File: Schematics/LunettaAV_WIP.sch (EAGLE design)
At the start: 64 parts, among them IC1 TLC339P, IC2 7805, IC3 4046N, IC4 4040N, IC5 4017N, IC6 4051N, IC7 4094N, IC8 4046N, IC9 40106N, J1 POWER_JACKPOWER_JACK_SLOT, U1 LM358, U2 LM358

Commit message: PT Delay and other fixes
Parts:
- removed JP7: (no value), pinhead:PINHD-1X3
- added C14: .1uF, capacitor-wima:C2.5/2
- added C15, C16, C17, C19, C20, C21, C22: 0.1uF, SparkFun-Capacitors:0.1UF-KIT-EZ-50V-20%
- added C18: 47uF, SparkFun-Capacitors:10UF-POLAR-RADIAL-2.5MM-25V-20%
- added C23: 100uF, SparkFun-Capacitors:100UF-POLAR-RADIAL-2.5MM-25V-20%
- added CLOCK-OUT, J3: WQP-PJ301M-12_JACK, MusicThingModular:WQP-PJ301M-12_JACK
- added D1: BAT42, diode:BAT42
- added J2: (no value), SparkFun-Connectors:CONN_04LONGPADS
- added R20: 10K, MusicThingModular:RESISTOR7MM
- added R21: (no value), MusicThingModular:RESISTOR7MM
- added VR5: (no value), MusicThingModular:9MM_SNAP-IN_POT_
- C1: value 10nF -> 0.1uF; device SparkFun-Capacitors:10NF-PTH-10MM-10000V-1-% -> SparkFun-Capacitors:0.1UF-KIT-EZ-50V-20%
- C10: value 10uF -> 10nF; device SparkFun-Capacitors:10UF-POLAR-RADIAL-2.5MM-25V-20% -> SparkFun-Capacitors:10NF-PTH-10MM-10000V-1-%
- C11: value 47uF -> 0.1uF; device SparkFun-Capacitors:10UF-POLAR-RADIAL-2.5MM-25V-20% -> SparkFun-Capacitors:0.1UF-KIT-EZ-50V-20%
- C2: value .1uF -> 10uF; device capacitor-wima:C2.5/2 -> SparkFun-Capacitors:10UF-POLAR-RADIAL-2.5MM-25V-20%
- C3: value 100uF -> 10uF; device SparkFun-Capacitors:100UF-POLAR-RADIAL-2.5MM-25V-20% -> SparkFun-Capacitors:10UF-POLAR-RADIAL-2.5MM-25V-20%
- C5: value 0.1uF -> 10uF; device SparkFun-Capacitors:0.1UF-KIT-EZ-50V-20% -> SparkFun-Capacitors:10UF-POLAR-RADIAL-2.5MM-25V-20%
- C8, C9: value 10uF -> 0.1uF; device SparkFun-Capacitors:10UF-POLAR-RADIAL-2.5MM-25V-20% -> SparkFun-Capacitors:0.1UF-KIT-EZ-50V-20%
- IC1: value TLC339P -> 7809\; device linear:TLC339P -> v-reg:78XXS
- IC10: value (none) -> 4051N; device v-reg:78XXS -> 40xx:4051N
- IC3: value 4046N -> 4040N; device 40xx:4046N -> 40xx:4040N
- IC4: value 4040N -> TLC339P; device 40xx:4040N -> linear:TLC339P
- IC5: value 4017N -> 4046N; device 40xx:4017N -> 40xx:4046N
- IC6: value 4051N -> 4094N; device 40xx:4051N -> 40xx:4094N
- IC7: value 4094N -> 40106N; device 40xx:4094N -> 40xx:40106N
- IC9: value 40106N -> 4017N; device 40xx:40106N -> 40xx:4017N
- JP1: device adafruit:PINHD-2X4 -> pinhead:PINHD-1X2
- JP2: device pinhead:PINHD-1X2 -> adafruit:PINHD-2X4
- JP4: device adafruit:PINHD-2X4 -> pinhead:PINHD-2X8
- JP5: device pinhead:PINHD-2X8 -> pinhead:PINHD-1X3
- R1, R2: value 10K -> 4.7K; device MusicThingModular:RESISTOR7MM -> MusicThingModular:RESISTOR10MM_RESISTOR
- R13: value (none) -> 1K
- R14: value 10K -> 1K
- R15: value 10K -> LDR; device MusicThingModular:RESISTOR7MM -> rcl:R-EU_0204/2V
- R16: value 10K -> 100k
- R17: value 1K -> 10k
- R18: value 10k -> 10K
- R19: value 100k -> 10K
- R22: value 1K -> (none)
- R23: value LDR -> (none); device rcl:R-EU_0204/2V -> MusicThingModular:RESISTOR7MM
- R3: value 10K -> 1K; device MusicThingModular:RESISTOR7MM -> MusicThingModular:RESISTOR10MM_RESISTOR
- R5: value 1K -> 10K; device MusicThingModular:RESISTOR10MM_RESISTOR -> MusicThingModular:RESISTOR7MM
- R6, R9: value 4.7K -> 10K; device MusicThingModular:RESISTOR10MM_RESISTOR -> MusicThingModular:RESISTOR7MM
- VR3: value (none) -> 100K
- VR4: value 100K -> (none)
- renumbered U$1 to OL96$1, U$2 to OL96$2
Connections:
- new net N$31: C19.2, DD1.11
- new net N$32: CLOCK-OUT.2, D1.C
- new net OUT: VR5.S
- net 3V3: now also C1.1, C4.1, R1.2, R2.2, R5.2; no longer C12.1, C13.1, R10.2, R11.2, R9.2
- net 5V: now also C23.+, C5.+, IC4A.-IN, IC4B.-IN, IC4C.-IN, IC4D.-IN, JP1.1; no longer C3.+, C9.+, IC1A.-IN, IC1B.-IN, IC1C.-IN, IC1D.-IN, JP2.1
- net 9V: now also C11.1, C12.1, C13.1, C15.1, C16.1, C17.1, C3.+, C6.1, C7.1, C8.1, C9.1, IC1.OUT, IC10P.VCC, IC4P.V+, IC6A.OE, IC6A.STR, IC6P.VDD, IC9P.VDD, R13.1; no longer C8.+, IC10.OUT, IC1P.V+, IC4P.VDD, IC6P.VCC, IC7A.OE, IC7A.STR, R22.1
- net ANALOGIN1: no longer U1G1.+IN
- net ANALOGIN2: now also U1G1.+IN
- net AUDIORATE: now also IC7C.O, IC9A.CLK; no longer IC5A.CLK, IC9C.O
- net BUFFCLOCK: now also IC6A.CLK, R22.1; no longer IC7A.CLK
- net BUFFMEL: now also R16.1, VR5.E; no longer R19.1
- net CLOCKSELECT: now also JP2.2, JP2.4, JP2.6, JP2.8; no longer JP4.2, JP4.4, JP4.6, JP4.8
- net DCIN: now also C2.+, IC1.IN; no longer C10.+, IC10.IN
- net DIN1: now also R3.2; no longer R5.2
- net GND: now also C1.2, C11.2, C14.2, C15.2, C16.2, C17.2, C18.-, C19.1, C2.-, C20.1, C22.2, C23.-, C5.-, C6.2, C7.2, C8.2, C9.2, CLOCK-OUT.1, DD1.12, IC1.GND, IC10A.INH, IC10P.GND, IC10P.VEE, IC4P.V-, IC5A.INH, IC6P.VSS, IC7D.I, IC7E.I, IC7F.I, IC9A.ENA, IC9P.VSS, R10.1, R11.1, R18.1, R19.1, R20.1, R23.2, R9.1, VR4.A, VR5.A; no longer C10.-, C11.-, C2.2, C5.1, C8.-, C9.-, IC10.GND, IC1P.V-, IC3A.INH, IC4P.VSS, IC5A.ENA, IC6A.INH, IC6P.GND, IC6P.VEE, IC9D.I, IC9E.I, IC9F.I, R1.1, R14.1, R15.1, R16.1, R2.1, R5.1
- net MELODYOUT: now also IC9A.Q0; no longer IC5A.Q0
- net MOOX: now also IC10A.C, JP5.3, R20.2; no longer IC6A.C, JP7.3, R16.2
- net MOXO: now also IC10A.B, JP5.2, R19.2; no longer IC6A.B, JP7.2, R15.2
- net MXOO: now also IC10A.A, JP5.1, R18.2; no longer IC6A.A, JP7.1, R14.2
- net N$1: now also JP1.2; no longer JP2.2
- net N$10: now also IC7B.O, IC7C.I; no longer IC9B.O, IC9C.I
- net N$11: now also C14.1, IC7A.I, R15.2, VR3.S; no longer C2.1, IC9A.I, R23.2, VR4.S
- net N$12: now also C21.1; no longer C6.1
- net N$13: now also R22.2, R23.1, U2G1.+IN; no longer C7.2, DD1.11
- net N$14: now also D1.A, U2G1.-IN, U2G1.OUT; no longer C7.1, DD1.12
- net N$15: now also R21.2; no longer R13.2
- net N$16: now also C18.+; no longer C11.+
- net N$17: now also C20.2; no longer C5.2
- net N$18: now also C22.1; no longer C4.1
- net N$19: now also IC10A.X, IC9A.RES; no longer IC5A.RES, IC6A.X
- net N$2: now also C10.2, IC5A.CX@2; no longer C1.2, IC3A.CX@2
- net N$20: now also IC10A.X0, IC9A.Q2; no longer IC5A.Q2, IC6A.X0
- net N$21: now also IC10A.X1, IC9A.Q3; no longer IC5A.Q3, IC6A.X1
- net N$22: now also IC10A.X2, IC9A.Q4; no longer IC5A.Q4, IC6A.X2
- net N$23: now also IC10A.X3, IC9A.Q5; no longer IC5A.Q5, IC6A.X3
- net N$24: now also IC10A.X4, IC9A.Q6; no longer IC5A.Q6, IC6A.X4
- net N$25: now also IC10A.X5, IC9A.Q7; no longer IC5A.Q7, IC6A.X5
- net N$26: now also IC10A.X6, IC9A.Q8; no longer IC5A.Q8, IC6A.X6
- net N$27: now also IC10A.X7, IC9A.Q9; no longer IC5A.Q9, IC6A.X7
- net N$28: now also IC6A.D, R14.1; no longer IC7A.D, R17.1
- net N$29: now also R16.2, R17.1; no longer R18.1, R19.2
- net N$3: now also R1.1; no longer R6.1
- net N$30: now also R17.2, VR4.S; no longer R18.2
- net N$4: now also R2.1; no longer R9.1
- net N$5: now also C10.1, IC5A.CX@1; no longer C1.1, IC3A.CX@1
- net N$6: now also IC5A.R1; no longer IC3A.R1
- net N$7: now also C21.2; no longer C6.2
- net N$8: now also R13.2; no longer R22.2
- net N$9: now also IC7A.O, IC7B.I, R15.1, VR3.E; no longer IC9A.O, IC9B.I, R23.1, VR4.E
- net OOX: now also IC4D.+IN, J2.4, R11.2; no longer IC1D.+IN, JP1.1, JP1.2, R8.2
- net OXO: now also IC4C.+IN, J2.3, R10.2; no longer IC1C.+IN, JP1.3, JP1.4, R3.2
- net PLL/16: now also IC3A.Q4; no longer IC4A.Q4
- net PLL/2: now also IC3A.Q1, JP2.3; no longer IC4A.Q1, JP4.3
- net PLL/32: now also IC3A.Q5; no longer IC4A.Q5
- net PLL/4: now also IC3A.Q2, JP2.5; no longer IC4A.Q2, JP4.5
- net PLL/8: now also IC3A.Q3, JP2.7; no longer IC4A.Q3, JP4.7
- net PLLCLOCKOUT: now also IC3A.P1, IC5A.VCOOUT, JP2.1; no longer IC3A.VCOOUT, IC4A.P1, JP4.1
- net RESET: now also IC4A.+IN, J2.1, R8.2; no longer IC1A.+IN, JP1.7, JP1.8, R1.2
- net SPEEDYBUFF: now also IC5A.VCOIN; no longer IC3A.VCOIN
- net SR1: now also IC6A.Q1, JP4.1, JP4.2; no longer IC7A.Q1, JP5.1, JP5.2
- net SR2: now also IC6A.Q2, JP4.3, JP4.4; no longer IC7A.Q2, JP5.3, JP5.4
- net SR3: now also IC6A.Q3, JP4.5, JP4.6; no longer IC7A.Q3, JP5.5, JP5.6
- net SR4: now also IC6A.Q4, JP4.7, JP4.8; no longer IC7A.Q4, JP5.7, JP5.8
- net SR5: now also IC6A.Q5, JP4.10, JP4.9; no longer IC7A.Q5, JP5.10, JP5.9
- net SR6: now also IC6A.Q6, JP4.11, JP4.12; no longer IC7A.Q6, JP5.11, JP5.12
- net SR7: now also IC6A.Q7, JP4.13, JP4.14; no longer IC7A.Q7, JP5.13, JP5.14
- net SR8: now also IC6A.Q8, JP4.15, JP4.16, R14.2; no longer IC7A.Q8, JP5.15, JP5.16, R17.2
- net TNSYOOX: now also IC4D.OUT, R7.1; no longer IC1D.OUT, R11.1
- net TNSYOXO: now also IC4C.OUT, R6.1; no longer IC1C.OUT, R10.1
- net TNSYRES: now also IC4A.OUT; no longer IC1A.OUT
- net TNSYXOO: now also IC4B.OUT, R5.1; no longer IC1B.OUT, R7.1
- net XOO: now also IC4B.+IN, J2.2, R9.2; no longer IC1B.+IN, JP1.5, JP1.6, R2.2
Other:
- note removed: "Buffer the Mix (LM358)"
- note removed: "Final Mix"
- note removed: "Send to PT2399"
- moved on the sheet: C1, IC3P, IC7P, IC8P, IC9P, R1, R10, R11, R13, R14, R15, R16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

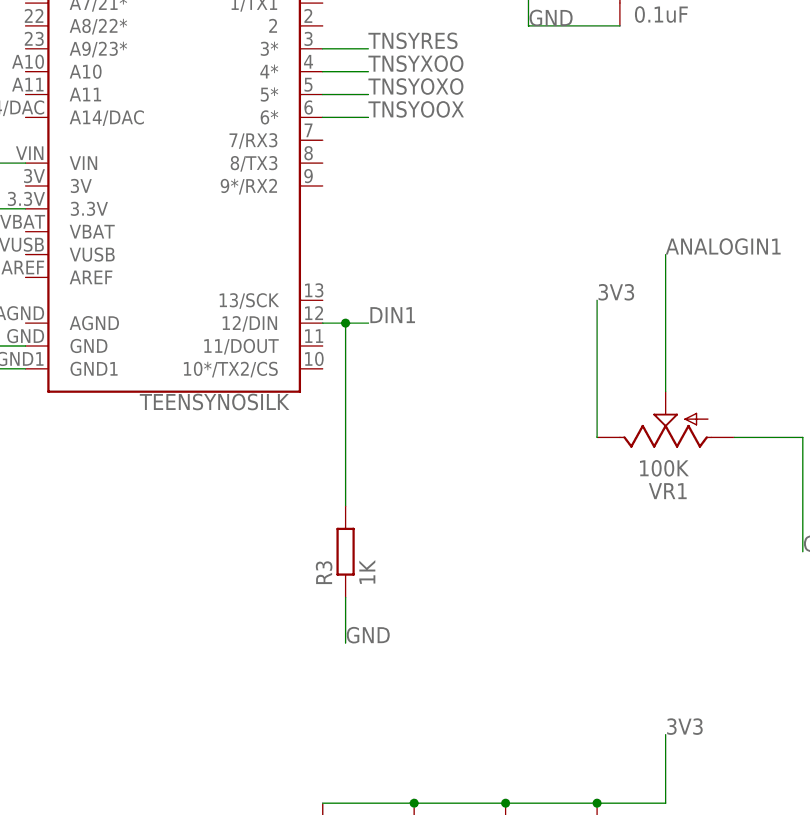
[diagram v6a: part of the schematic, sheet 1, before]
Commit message: update schematics to match new code
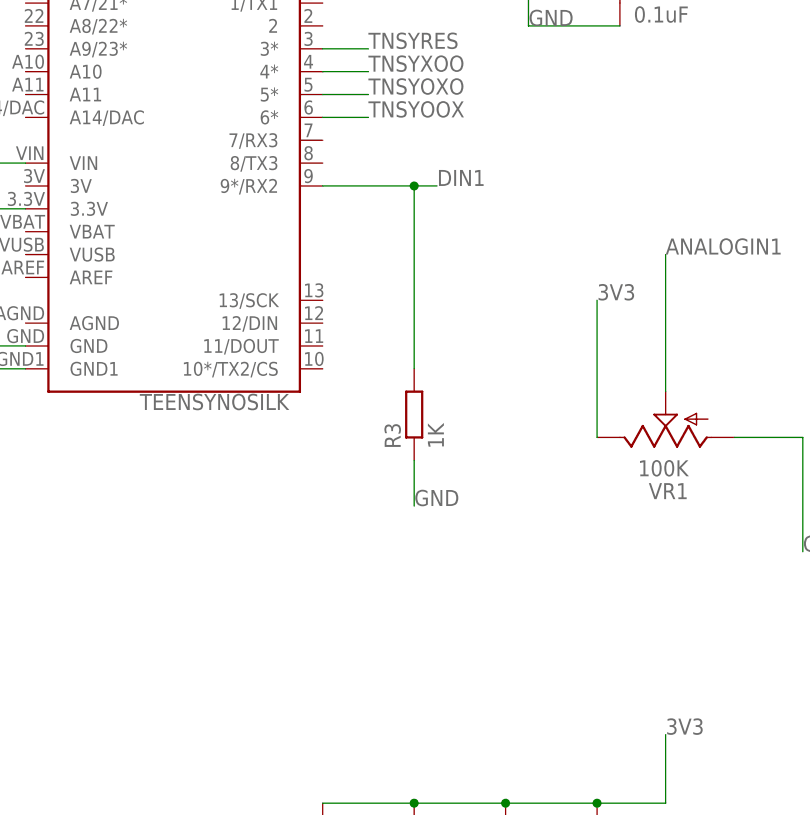
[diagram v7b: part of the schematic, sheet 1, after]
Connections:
- net DIN1: now also B1.9*/RX2; no longer B1.12/DIN
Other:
- moved on the sheet: R3
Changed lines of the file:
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@@
 <attribute name="VALUE" x="35.56" y="60.96" size="1.778" layer="96" rot="R180"/>
 </instance>
-<instance part="R3" gate="G$1" x="-35.56" y="50.8" smashed="yes" rot="R90">
-<attribute name="NAME" x="-37.0586" y="46.99" size="1.778" layer="95" rot="R90"/>
-<attribute name="VALUE" x="-32.258" y="46.99" size="1.778" layer="96" rot="R90"/>
+<instance part="R3" gate="G$1" x="-27.94" y="66.04" smashed="yes" rot="R90">
+<attribute name="NAME" x="-29.4386" y="62.23" size="1.778" layer="95" rot="R90"/>
+<attribute name="VALUE" x="-24.638" y="62.23" size="1.778" layer="96" rot="R90"/>
 </instance>
 <instance part="FRAME1" gate="G$1" x="-142.24" y="-76.2" smashed="yes">
@@
 <segment>
 <pinref part="R3" gate="G$1" pin="1"/>
-<wire x1="-35.56" y1="45.72" x2="-35.56" y2="40.64" width="0.1524" layer="91"/>
-<label x="-35.56" y="40.64" size="1.778" layer="95"/>
+<wire x1="-27.94" y1="60.96" x2="-27.94" y2="55.88" width="0.1524" layer="91"/>
+<label x="-27.94" y="55.88" size="1.778" layer="95"/>
 </segment>
 <segment>
@@
 <net name="DIN1" class="0">
 <segment>
-<pinref part="B1" gate="G$1" pin="12/DIN"/>
-<wire x1="-38.1" y1="76.2" x2="-35.56" y2="76.2" width="0.1524" layer="91"/>
-<label x="-33.02" y="76.2" size="1.778" layer="95"/>
+<label x="-25.4" y="91.44" size="1.778" layer="95"/>
 <pinref part="R3" gate="G$1" pin="2"/>
-<wire x1="-35.56" y1="76.2" x2="-33.02" y2="76.2" width="0.1524" layer="91"/>
-<wire x1="-35.56" y1="55.88" x2="-35.56" y2="76.2" width="0.1524" layer="91"/>
-<junction x="-35.56" y="76.2"/>
-</segment>
-<segment>
+<wire x1="-27.94" y1="91.44" x2="-25.4" y2="91.44" width="0.1524" layer="91"/>
+<wire x1="-27.94" y1="71.12" x2="-27.94" y2="91.44" width="0.1524" layer="91"/>
+<pinref part="B1" gate="G$1" pin="9*/RX2"/>
+<wire x1="-27.94" y1="91.44" x2="-38.1" y2="91.44" width="0.1524" layer="91"/>
+<junction x="-27.94" y="91.44"/>
+</segment>
+<segment>

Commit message: finish schematics?
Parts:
- removed VR2, VR3: 100K, MusicThingModular:9MM_SNAP-IN_POT_
- added C24: 10uF, SparkFun-Capacitors:10UF-POLAR-RADIAL-2.5MM-25V-20%
- added D2: BAT42, diode:BAT42
- added DENSITY, PITCH, SPEED: 100K, MusicThingModular:9MM_SNAP-IN_POT_
- added LED1, LED2: (no value), led:LED3MM
- added R24, R25, R26: 4.7k, MusicThingModular:RESISTOR7MM
- added R27, R28, R30, R31: 100k, MusicThingModular:RESISTOR7MM
- added R29, R32: 10k, MusicThingModular:RESISTOR7MM
- added T1, T2: (no value), transistor-neu-to92:2N4401-NPN-TO92-EBC
- added U3: MICROCHIP_MCP41050-I-PMICROCHIP_MCP41050-I-P_0_0, MCP41050:MICROCHIP_MCP41050-I-PMICROCHIP_MCP41050-I-P_0_0
- C10: value 10nF -> 0.1uF; device SparkFun-Capacitors:10NF-PTH-10MM-10000V-1-% -> SparkFun-Capacitors:0.1UF-KIT-EZ-50V-20%
- JP5: device pinhead:PINHD-1X3 -> jumper:JP4E
- R1, R2, R3: device MusicThingModular:RESISTOR10MM_RESISTOR -> MusicThingModular:RESISTOR7MM
- R21: value (none) -> 2.2k
- R22, R23: value (none) -> 100k
- VR1: value 100K -> (none); device MusicThingModular:9MM_SNAP-IN_POT_ -> MusicThingModular:BOURNS_3362P_TRIMMERP
- renumbered VR4 to FDBCK, VR5 to MIX
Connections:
- new net DPOTDATA: B1.11/DOUT, R25.1, U3.SI
- new net DPOTSCK: B1.13/SCK, R26.1, U3.SCK
- new net DPOTSEL: B1.10*/TX2/CS, R24.1, U3.!CS!
- new net LDRIVER: JP5.4, R30.1
- new net N$33: R21.1, U3.PA0
- new net N$34: R27.2, R28.2, T1.B
- new net N$35: R29.1, T1.C
- new net N$36: LED1.C, R29.2
- new net N$37: R30.2, R31.2, T2.B
- new net N$38: R32.1, T2.C
- new net N$39: LED2.C, R32.2
- new net N$40: J3.2, VR1.2
- new net N$41: C24.-, VR1.1
- net 3V3: now also DENSITY.E, SPEED.E; no longer VR1.E, VR2.E
- net 5V: now also R24.2, R25.2, R26.2, U3.VDD
- net 9V: now also LED1.A, LED2.A
- net ANALOGIN1: now also DENSITY.S; no longer VR1.S
- net ANALOGIN2: now also SPEED.S; no longer VR2.S
- net BUFFCLOCK: now also R27.1
- net GND: now also D2.A, DENSITY.A, J3.1, R28.1, R31.1, SPEED.A, T1.E, T2.E, U3.PB0, U3.PW0, U3.VSS, VR1.3; no longer VR1.A, VR2.A
- net N$11: now also PITCH.S; no longer VR3.S
- net N$32: now also D2.C
- net N$9: now also PITCH.E; no longer VR3.E
- net OUT: now also C24.+
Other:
- moved on the sheet: C14, C2, C3, C5, CLOCK-OUT, IC1, IC2, IC7A, IC7B, IC7C, IC7D, IC7E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
